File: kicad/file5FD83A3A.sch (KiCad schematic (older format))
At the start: 25 parts, among them SW1 RESET, U2 STM32F439VITx, Y1 NX3225GD-8.000M-EXS00A-CG04874

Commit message: Power reg U2/U3 and supporting components
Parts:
- renumbered U2 to U4
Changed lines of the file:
@@
 P 8500 6450
 AR Path="/5FDCA4A8" Ref="U?"  Part="1"
-AR Path="/5FD83A3B/5FDCA4A8" Ref="U2"  Part="1"
-F 0 "U2" H 8500 6500 50  0000 C CNN
+AR Path="/5FD83A3B/5FDCA4A8" Ref="U4"  Part="1"
+F 0 "U4" H 8500 6500 50  0000 C CNN
 F 1 "STM32F439VITx" H 8500 6400 50  0000 C CNN
 F 2 "Package_QFP:LQFP-100_14x14mm_P0.5mm" H 7800 3850 50  0001 R CNN

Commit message: Power reg Section 1 initial entry; annotate
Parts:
- renumbered U4 to IC3
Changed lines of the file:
@@
 P 8500 6450
 AR Path="/5FDCA4A8" Ref="U?"  Part="1"
-AR Path="/5FD83A3B/5FDCA4A8" Ref="U4"  Part="1"
-F 0 "U4" H 8500 6500 50  0000 C CNN
+AR Path="/5FD83A3B/5FDCA4A8" Ref="IC3"  Part="1"
+F 0 "IC3" H 8500 6500 50  0000 C CNN
 F 1 "STM32F439VITx" H 8500 6400 50  0000 C CNN
 F 2 "Package_QFP:LQFP-100_14x14mm_P0.5mm" H 7800 3850 50  0001 R CNN

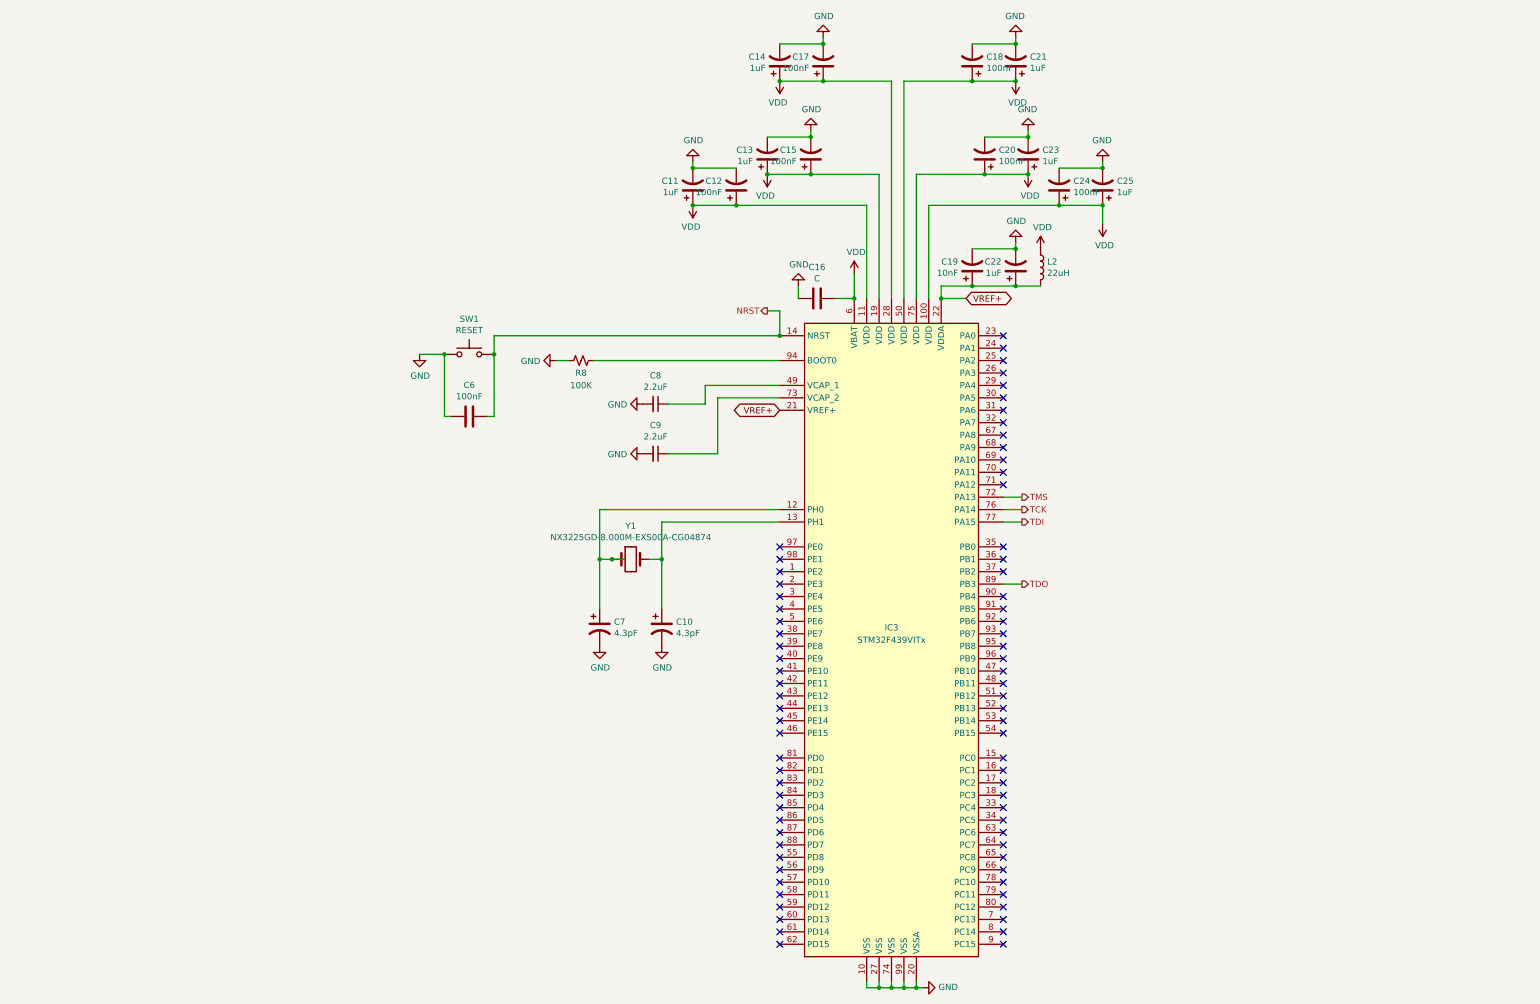
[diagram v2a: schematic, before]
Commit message: Ethernet initial schematic; start ERC
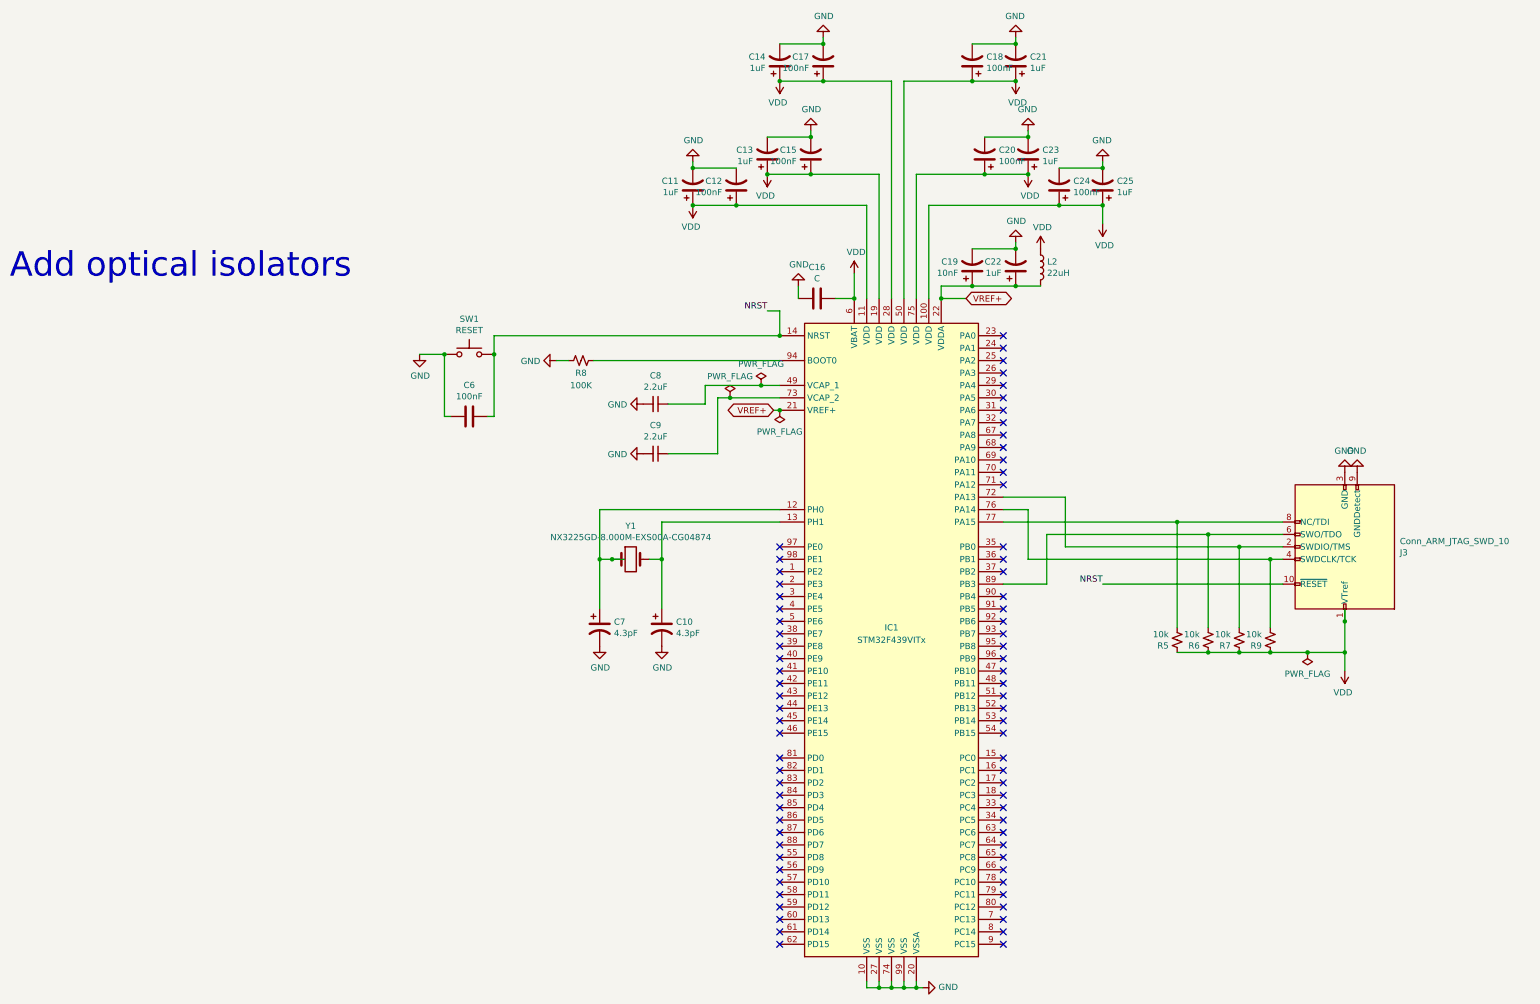
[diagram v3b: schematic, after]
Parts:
- added J3: Conn_ARM_JTAG_SWD_10, symbol Connector:Conn_ARM_JTAG_SWD_10
- added R5, R6, R7, R9: 10k, symbol Device:R_Small_US
- renumbered IC3 to IC1
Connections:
- net GND: now also J3.3 (GND), J3.5 (GND), J3.9 (GNDDetect)
- net NRST: now also J3.10 (~RESET~)
- net VDD: now also J3.1 (VTref), R5.1, R6.1, R7.1, R9.1
- net TCK: no longer names the net of IC1.76 (PA14)
- net TCK: now also J3.4 (SWDCLK/TCK), R9.2
- net TDI: no longer names the net of IC1.77 (PA15)
- net TDI: now also J3.8 (NC/TDI), R5.2
- net TDO: no longer names the net of IC1.89 (PB3)
- net TDO: now also J3.6 (SWO/TDO), R6.2
- net TMS: no longer names the net of IC1.72 (PA13)
- net TMS: now also J3.2 (SWDIO/TMS), R7.2
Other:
- note added: "Add optical isolators"
